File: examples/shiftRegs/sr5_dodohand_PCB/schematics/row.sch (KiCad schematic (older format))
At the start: 5 parts, among them U2 LMC7101, U3 LMC7101, U4 SN74AHC1G125

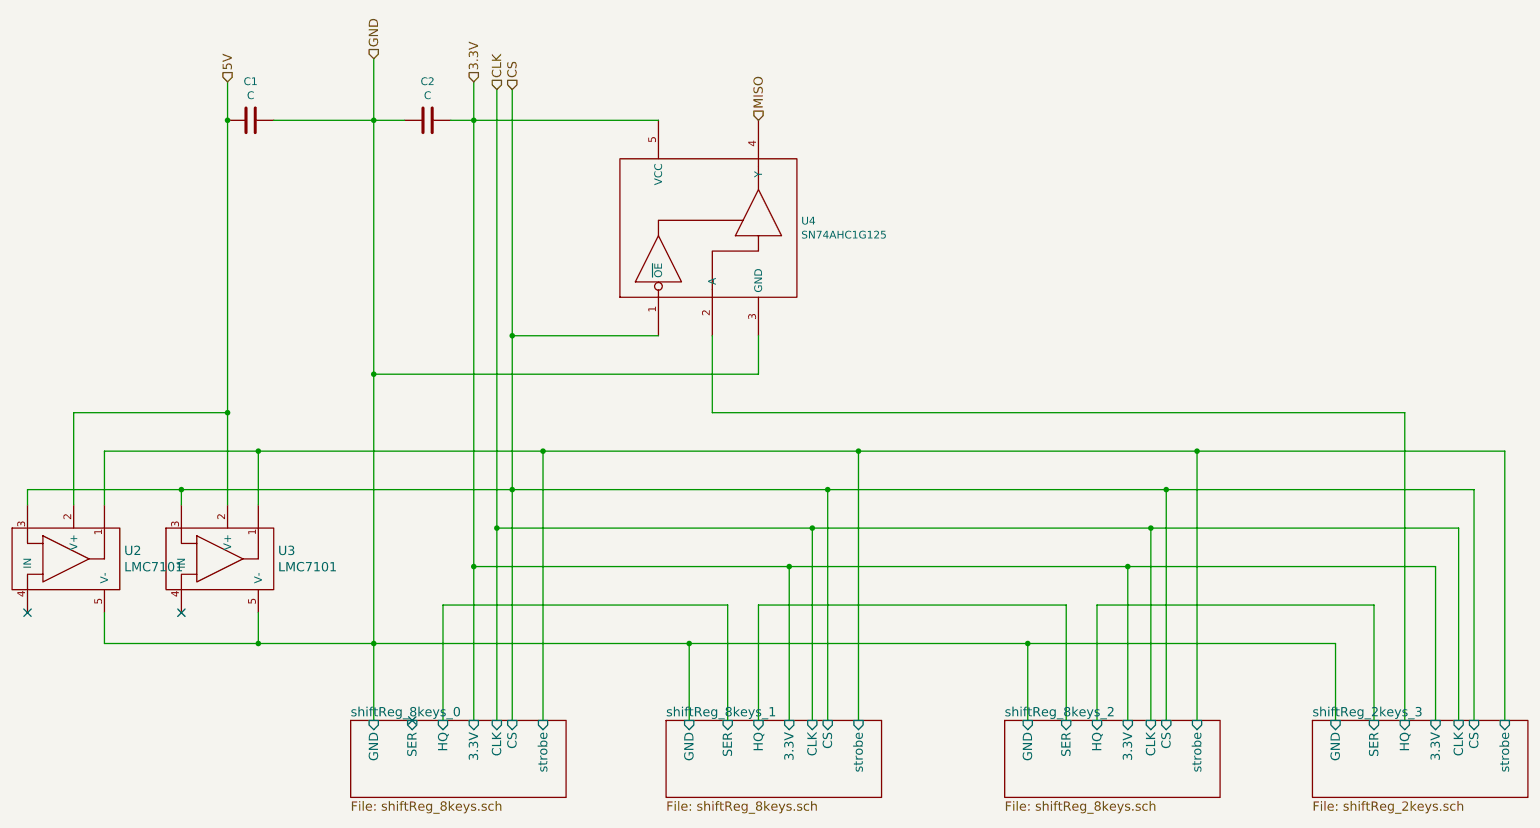
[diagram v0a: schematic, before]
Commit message: updated dodoHand shift-register schematics
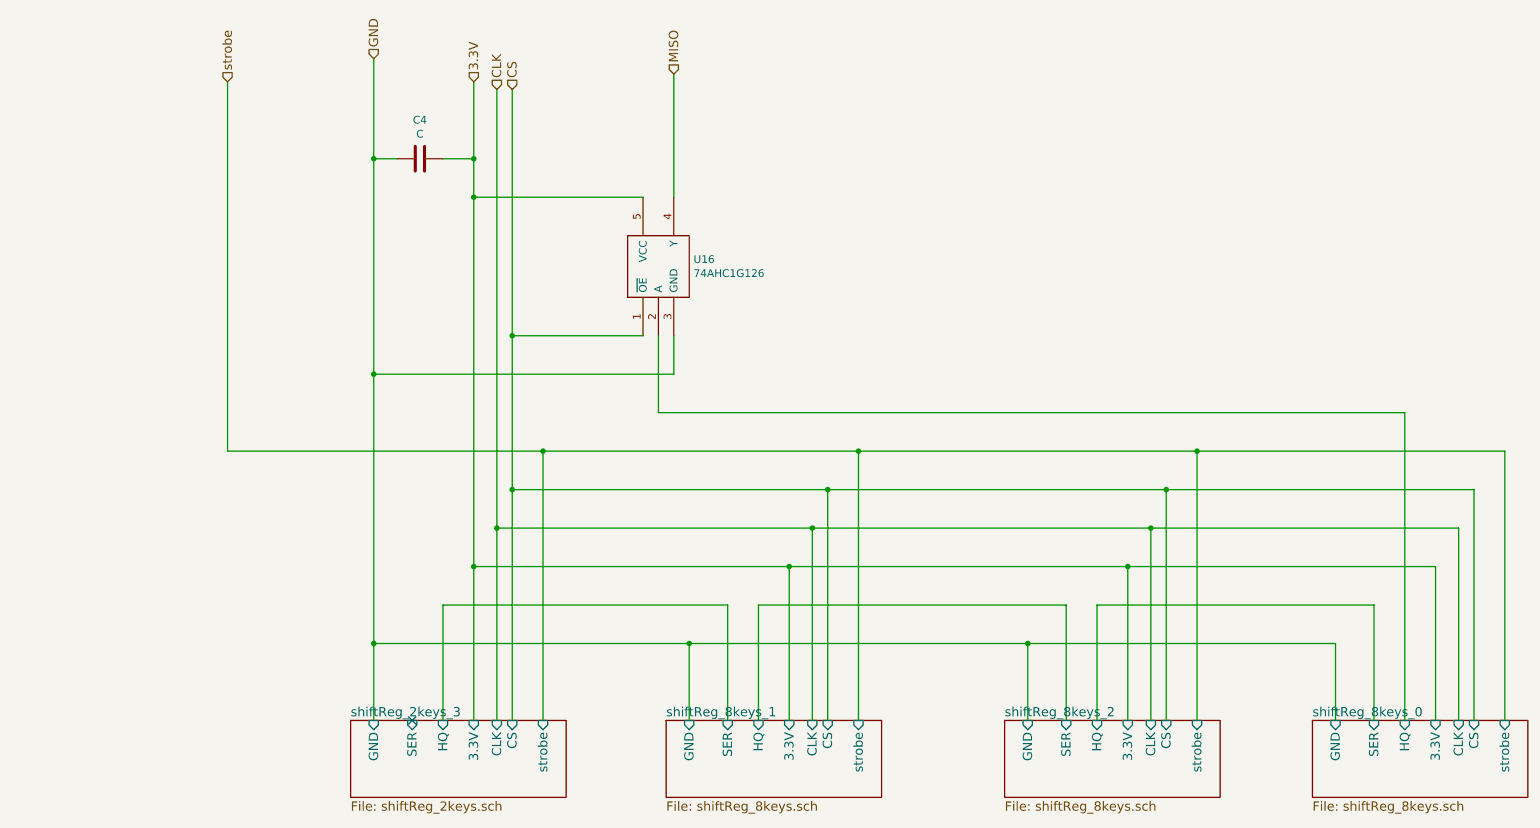
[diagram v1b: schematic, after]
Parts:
- removed C1: C, symbol C
- removed U2, U3: LMC7101, symbol LMC7101
- removed U4: SN74AHC1G125, symbol SN74AHC1G125
- added U11: 74AHC1G126, symbol 74AHC1G126
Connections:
- net 3.3V: now also U11.5 (VCC)
- net CS: now also U11.1 (~OE)
- net GND: now also U11.3 (GND)
- net MISO: now also U11.4 (Y)
- net shiftReg_8keys_0/HQ: now also U11.2 (A)
- no-connect marks 3 -> 1
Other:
- moved on the sheet: C4
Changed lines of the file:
@@
 EESchema Schematic File Version 2
-LIBS:DH_component
+LIBS:dodohand_PCB-rescue
 LIBS:power
 LIBS:device
@@
 LIBS:contrib
 LIBS:valves
+LIBS:DH_component
+LIBS:strobe_buffer
 LIBS:dodohand_PCB-cache
 EELAYER 25 0
@@
 Title "Row of shift registers with 26 keys"
 Date ""
-Rev ""
+Rev "1"
 Comp "wolfv"
-Comment1 ""
+Comment1 "74HC165 with unconnected SER pin has unused input pins."
 Comment2 ""
 Comment3 ""
 Comment4 ""
 $EndDescr
-$Comp
-L SN74AHC1G125 U4
-U 1 1 5809E85F
-P 5500 1950
-AR Path="/5809DAC4/5809E85F" Ref="U4"  Part="1"
-AR Path="/580AEA89/5809E85F" Ref="U11"  Part="1"
-F 0 "U4" V 5296 1372 50  0000 R CNN
-F 1 "SN74AHC1G125" V 5205 1372 50  0000 R CNN
-F 2 "" H 5350 1950 50  0000 C CNN
-F 3 "" H 5350 1950 50  0000 C CNN
-	1    5500 1950
-	0    -1   -1   0
-$EndComp
 Text HLabel 3950 1250 1    60   Input ~ 0
 3.3V
-Text HLabel 5800 1500 1    60   Input ~ 0
+Text HLabel 5250 1200 1    60   Input ~ 0
 MISO
 Text HLabel 2350 1250 1    60   Input ~ 0
-5V
+strobe
 Text HLabel 3300 1100 1    60   Input ~ 0
 GND
@@
 L C C2
 U 1 1 580B7854
-P 3650 1500
+P 3600 1750
 AR Path="/5809DAC4/580B7854" Ref="C2"  Part="1"
 AR Path="/580AEA89/580B7854" Ref="C4"  Part="1"
-F 0 "C2" V 3398 1500 50  0000 C CNN
-F 1 "C" V 3489 1500 50  0000 C CNN
-F 2 "" H 3688 1350 50  0000 C CNN
-F 3 "" H 3650 1500 50  0000 C CNN
-	1    3650 1500
+F 0 "C4" V 3348 1750 50  0000 C CNN
+F 1 "C" V 3439 1750 50  0000 C CNN
+F 2 "" H 3638 1600 50  0000 C CNN
+F 3 "" H 3600 1750 50  0000 C CNN
+	1    3600 1750
 	0    1    1    0
 $EndComp
-$Comp
-L C C1
-U 1 1 5816B63F
-P 2500 1500
-AR Path="/5809DAC4/5816B63F" Ref="C1"  Part="1"
-AR Path="/580AEA89/5816B63F" Ref="C3"  Part="1"
-F 0 "C1" V 2248 1500 50  0000 C CNN
-F 1 "C" V 2339 1500 50  0000 C CNN
-F 2 "" H 2538 1350 50  0000 C CNN
-F 3 "" H 2500 1500 50  0000 C CNN
-	1    2500 1500
-	0    1    1    0
-$EndComp
-$Sheet
-S 3150 5400 1400 500
+$Sheet
+S 9400 5400 1400 500
 U 58184E06
 F0 "shiftReg_8keys_0" 60
 F1 "shiftReg_8keys.sch" 60
-F2 "strobe" I T 4400 5400 60
-F3 "GND" I T 3300 5400 60
-F4 "HQ" I T 3750 5400 60
-F5 "SER" I T 3550 5400 60
-F6 "3.3V" I T 3950 5400 60
-F7 "CLK" I T 4100 5400 60
-F8 "CS" I T 4200 5400 60
-$EndSheet
-$Comp
-L LMC7101 U3
-U 1 1 5813762C
-P 2150 4350
-AR Path="/5809DAC4/5813762C" Ref="U3"  Part="1"
-AR Path="/580AEA89/5813762C" Ref="U10"  Part="1"
-F 0 "U3" V 2097 4878 60  0000 L CNN
-F 1 "LMC7101" V 2203 4878 60  0000 L CNN
-F 2 "" H 2150 4350 60  0001 C CNN
-F 3 "" H 2150 4350 60  0001 C CNN
-	1    2150 4350
-	0    1    1    0
-$EndComp
-NoConn ~ 2050 4700
-Wire Wire Line
-	3800 1500 5150 1500
+F2 "strobe" I T 10650 5400 60
+F3 "GND" I T 9550 5400 60
+F4 "HQ" I T 10000 5400 60
+F5 "SER" I T 9800 5400 60
+F6 "3.3V" I T 10200 5400 60
+F7 "CLK" I T 10350 5400 60
+F8 "CS" I T 10450 5400 60
+$EndSheet
+Wire Wire Line
+	3950 2000 5050 2000
 Connection ~ 4200 3900
 Wire Wire Line
 	4200 1300 4200 5400
-Connection ~ 3950 1500
+Connection ~ 3950 2000
 Connection ~ 3950 4400
 Connection ~ 4100 4150
@@
 	6250 3900 6250 5400
 Wire Wire Line
-	1050 3900 10450 3900
+	4200 3900 10450 3900
 Wire Wire Line
 	4100 4150 10350 4150
@@
 	5350 4900 5350 5400
 Wire Wire Line
-	1550 4900 9550 4900
-Wire Wire Line
 	3300 1100 3300 5400
 Wire Wire Line
-	5800 3150 5800 2900
-Wire Wire Line
-	2650 1500 3500 1500
-Connection ~ 3300 1500
-Connection ~ 2350 1500
-Wire Wire Line
-	5150 2900 4200 2900
+	5250 3150 5250 2900
+Wire Wire Line
+	3300 1750 3450 1750
+Connection ~ 3300 1750
+Wire Wire Line
+	5050 2900 4200 2900
 Connection ~ 4200 2900
 Wire Wire Line
-	2550 4900 2550 4700
-Wire Wire Line
-	2350 1250 2350 4000
-Wire Wire Line
-	2050 4000 2050 3900
-Wire Wire Line
-	3300 3150 5800 3150
+	2350 1250 2350 3650
+Wire Wire Line
+	3300 3150 5250 3150
 Connection ~ 3300 3150
-Wire Wire Line
-	2550 4000 2550 3650
-Wire Wire Line
-	1550 3650 10650 3650
 Wire Wire Line
 	4400 3650 4400 5400
@@
 $EndSheet
 Wire Wire Line
-	5500 2900 5500 3400
-Wire Wire Line
-	5500 3400 10000 3400
+	5150 2900 5150 3400
+Wire Wire Line
+	5150 3400 10000 3400
 Wire Wire Line
 	6450 3650 6450 5400
@@
 $EndSheet
 $Sheet
-S 9400 5400 1400 500
+S 3150 5400 1400 500
 U 580FCD1C
 F0 "shiftReg_2keys_3" 60
 F1 "shiftReg_2keys.sch" 60
-F2 "strobe" I T 10650 5400 60
-F3 "GND" I T 9550 5400 60
-F4 "HQ" I T 10000 5400 60
-F5 "SER" I T 9800 5400 60
-F6 "3.3V" I T 10200 5400 60
-F7 "CLK" I T 10350 5400 60
-F8 "CS" I T 10450 5400 60
+F2 "strobe" I T 4400 5400 60
+F3 "GND" I T 3300 5400 60
+F4 "HQ" I T 3750 5400 60
+F5 "SER" I T 3550 5400 60
+F6 "3.3V" I T 3950 5400 60
+F7 "CLK" I T 4100 5400 60
+F8 "CS" I T 4200 5400 60
 $EndSheet
 Wire Wire Line
@@
 	9550 4900 9550 5400
 Wire Wire Line
-	7550 5400 7550 4900
+	7550 4900 7550 5400
 Connection ~ 7550 4900
 Wire Wire Line
@@
 	8650 3650 8650 5400
 Connection ~ 8650 3650
+Wire Wire Line
+	2350 3650 10650 3650
+Wire Wire Line
+	3300 4900 9550 4900
 $Comp
-L LMC7101 U2
-U 1 1 5810E0C5
-P 1150 4350
-AR Path="/5809DAC4/5810E0C5" Ref="U2"  Part="1"
-AR Path="/580AEA89/5810E0C5" Ref="U9"  Part="1"
-F 0 "U2" V 1097 4878 60  0000 L CNN
-F 1 "LMC7101" V 1203 4878 60  0000 L CNN
-F 2 "" H 1150 4350 60  0001 C CNN
-F 3 "" H 1150 4350 60  0001 C CNN
-	1    1150 4350
-	0    1    1    0
+L 74AHC1G126 U11
+U 1 1 582FA7A2
+P 5150 2450
+AR Path="/5809DAC4/582FA7A2" Ref="U11"  Part="1"
+AR Path="/580AEA89/582FA7A2" Ref="U16"  Part="1"
+F 0 "U16" V 5196 2222 50  0000 R CNN
+F 1 "74AHC1G126" V 5105 2222 50  0000 R CNN
+F 2 "" H 5000 2200 50  0000 C CNN
+F 3 "" H 5000 2200 50  0000 C CNN
+	1    5150 2450
+	0    -1   -1   0
 $EndComp
 Wire Wire Line
-	1050 3900 1050 4000
-Connection ~ 2050 3900
-Wire Wire Line
-	2350 3400 1350 3400
-Wire Wire Line
-	1350 3400 1350 4000
-Connection ~ 2350 3400
-Wire Wire Line
-	1550 4900 1550 4700
-Connection ~ 2550 4900
-NoConn ~ 1050 4700
-Wire Wire Line
-	1550 3650 1550 4000
-Connection ~ 2550 3650
+	5250 2000 5250 1200
+Wire Wire Line
+	3750 1750 3950 1750
+Connection ~ 3950 1750
 $EndSCHEMATC
